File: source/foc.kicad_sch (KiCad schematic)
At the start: 22 parts

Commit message: Add files via upload
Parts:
- gave numbers to parts that had none: 22
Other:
- sheet mcu ports: added none; removed ADC_15, ADC_TEMP2, ADC_TEMP3, MISO_ADC_EXT2, PC10_UART_TX, PC11_UART_RX, PC12, PC9, RX_SDA_NSS, SCK_ADC_EXT, TX_SCL_MOSI

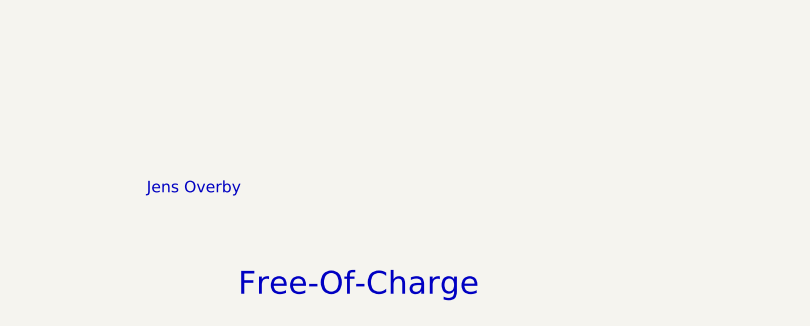
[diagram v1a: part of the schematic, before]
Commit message: Changes suggested by mxlemming, Elwin and hackey on Discord
New power supplies and using other op-amps for current sense
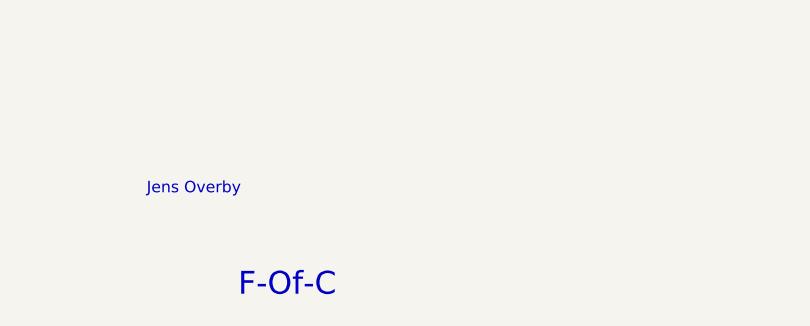
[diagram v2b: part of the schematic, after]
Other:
- note added: "F-Of-C"
- note removed: "Free-Of-Charge"

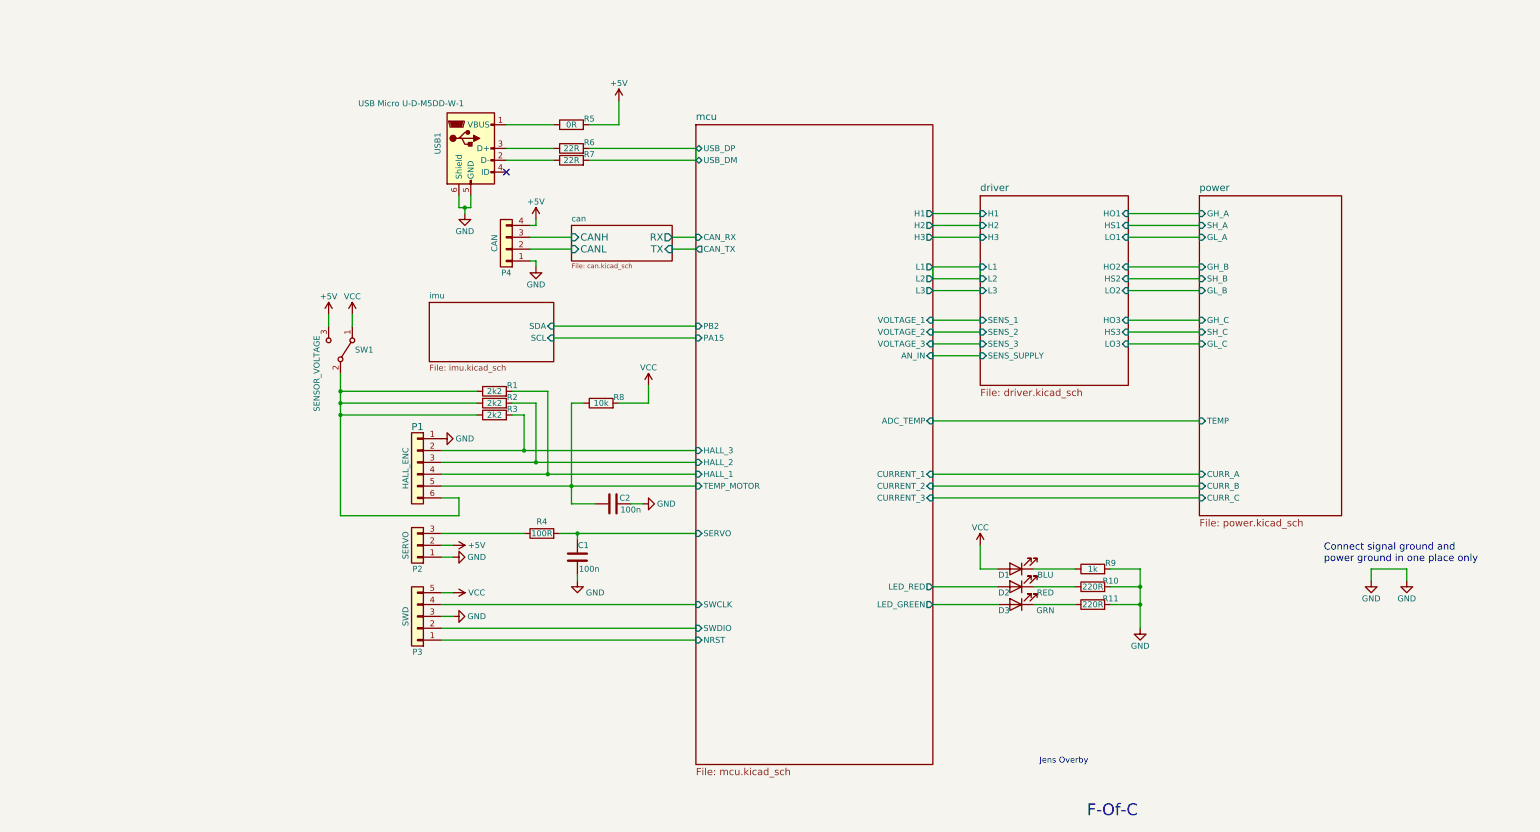
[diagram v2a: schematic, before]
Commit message: First attempt of layout
It's a rats nest. Will have to remove some connections temporarily for the first prototype.
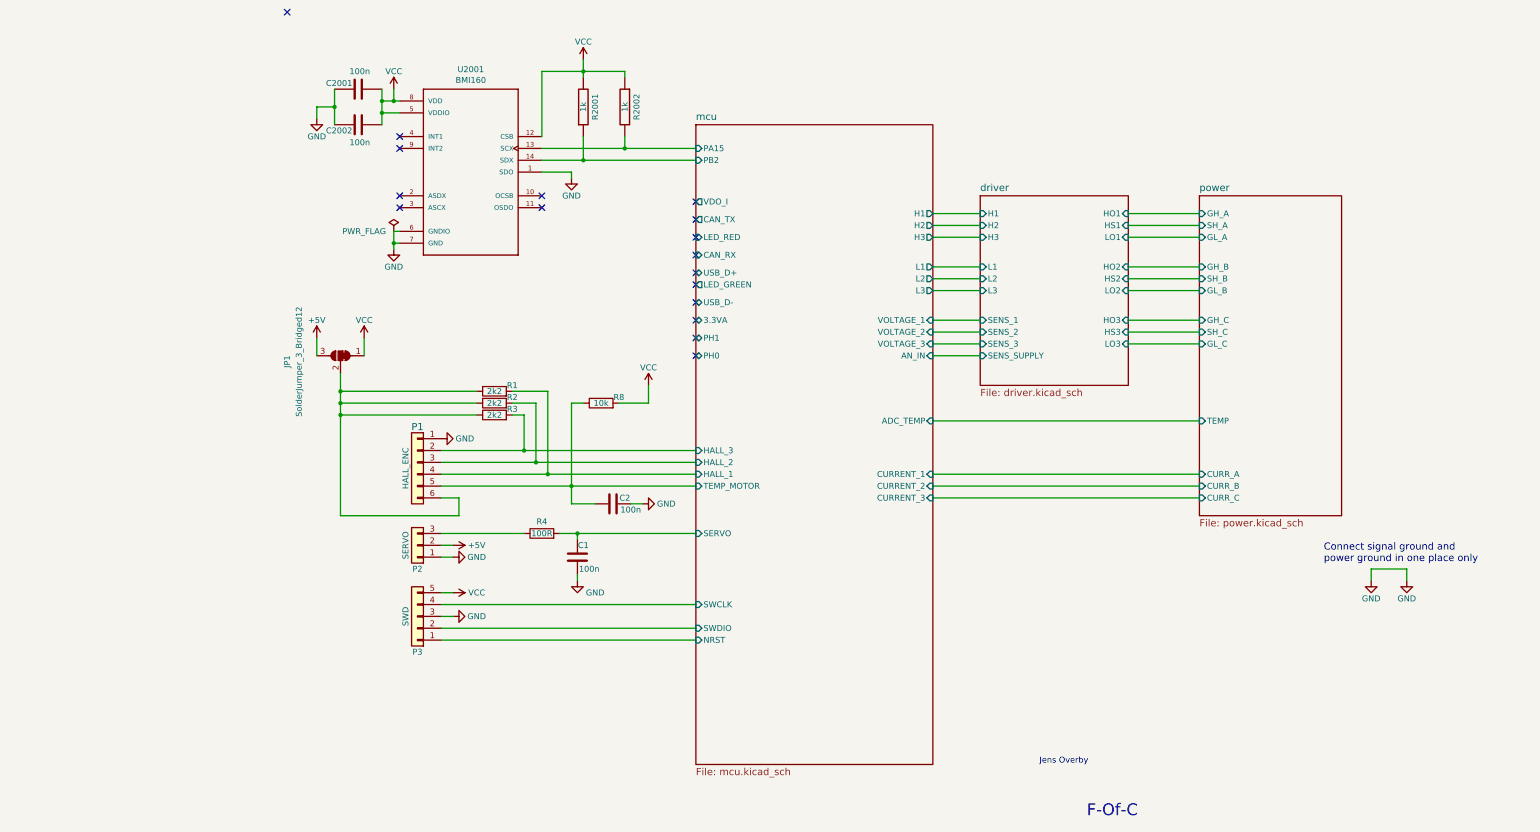
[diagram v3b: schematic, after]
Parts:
- removed D1: BLU, LED_SMD:LED_0603_1608Metric, symbol Device:LED
- removed D2: RED, LED_SMD:LED_0603_1608Metric, symbol Device:LED
- removed D3: GRN, LED_SMD:LED_0603_1608Metric, symbol Device:LED
- removed P4: CAN, symbol Connector_Generic:Conn_01x04
- removed R10, R11: 220R, symbol Device:R
- removed R5: 0R, symbol Device:R
- removed R6, R7: 22R, symbol Device:R
- removed R9: 1k, symbol Device:R
- removed SW1: SENSOR_VOLTAGE, Button_Switch_THT:SW_E-Switch_EG1224_SPDT_Angled, symbol Switch:SW_SPDT
- removed USB1: USB Micro U-D-M5DD-W-1, Connector_USB:USB_Micro-B_Wuerth_614105150721_Vertical, symbol Connector:USB_B_Micro
- added C2001, C2002: 100n, Capacitor_SMD:C_0603_1608Metric, symbol BLDC_4-rescue:C-RESCUE-BLDC_4
- added JP1: SolderJumper_3_Bridged12, Jumper:SolderJumper-3_P1.3mm_Bridged12_RoundedPad1.0x1.5mm_NumberLabels, symbol Jumper:SolderJumper_3_Bridged12
- added R2001, R2002: 1k, Resistor_SMD:R_0402_1005Metric, symbol BLDC_4-rescue:R-RESCUE-BLDC_4
- added U2001: BMI160, Package_LGA:Bosch_LGA-14_3x2.5mm_P0.5mm, symbol Cheap-FOCer-2-60mm-rescue:BMI160-IMU
- C1, C2: footprint (none) -> Capacitor_SMD:C_0603_1608Metric
- P1: footprint Connector_JST:JST_PH_B6B-PH-K_1x06_P2.00mm_Vertical -> Connector_PinHeader_2.54mm:PinHeader_1x06_P2.54mm_Vertical
- P2: footprint (none) -> Connector_PinHeader_2.54mm:PinHeader_1x03_P2.54mm_Vertical
- P3: footprint (none) -> Connector_PinHeader_2.54mm:PinHeader_1x05_P2.54mm_Vertical
- R1, R2, R3, R4, R8: footprint (none) -> Resistor_SMD:R_0402_1005Metric
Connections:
- net +5V: now also JP1.3 (B)
- net GND: now also C2001.1, C2002.1, U2001.1 (SDO), U2001.6 (GNDIO), U2001.7 (GND)
- net VCC: now also C2001.2, C2002.2, JP1.1 (A), R2001.2, R2002.1, U2001.12 (CSB), U2001.5 (VDDIO), U2001.8 (VDD)
- net at P1.6 (Pin_6), R1.1, R2.1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: now also JP1.2 (C)
- new net mcu/PA15: R2002.2, U2001.13 (SCX)
- new net mcu/PB2: R2001.1, U2001.14 (SDX)
- no-connect marks 1 -> 17
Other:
- removed sheet can
- removed sheet imu
- sheet mcu ports: added 3.3VA, PH0, PH1, USB_D+, USB_D-, VDO_I; removed USB_DM, USB_DP

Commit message: Most components now jlcpcb basic
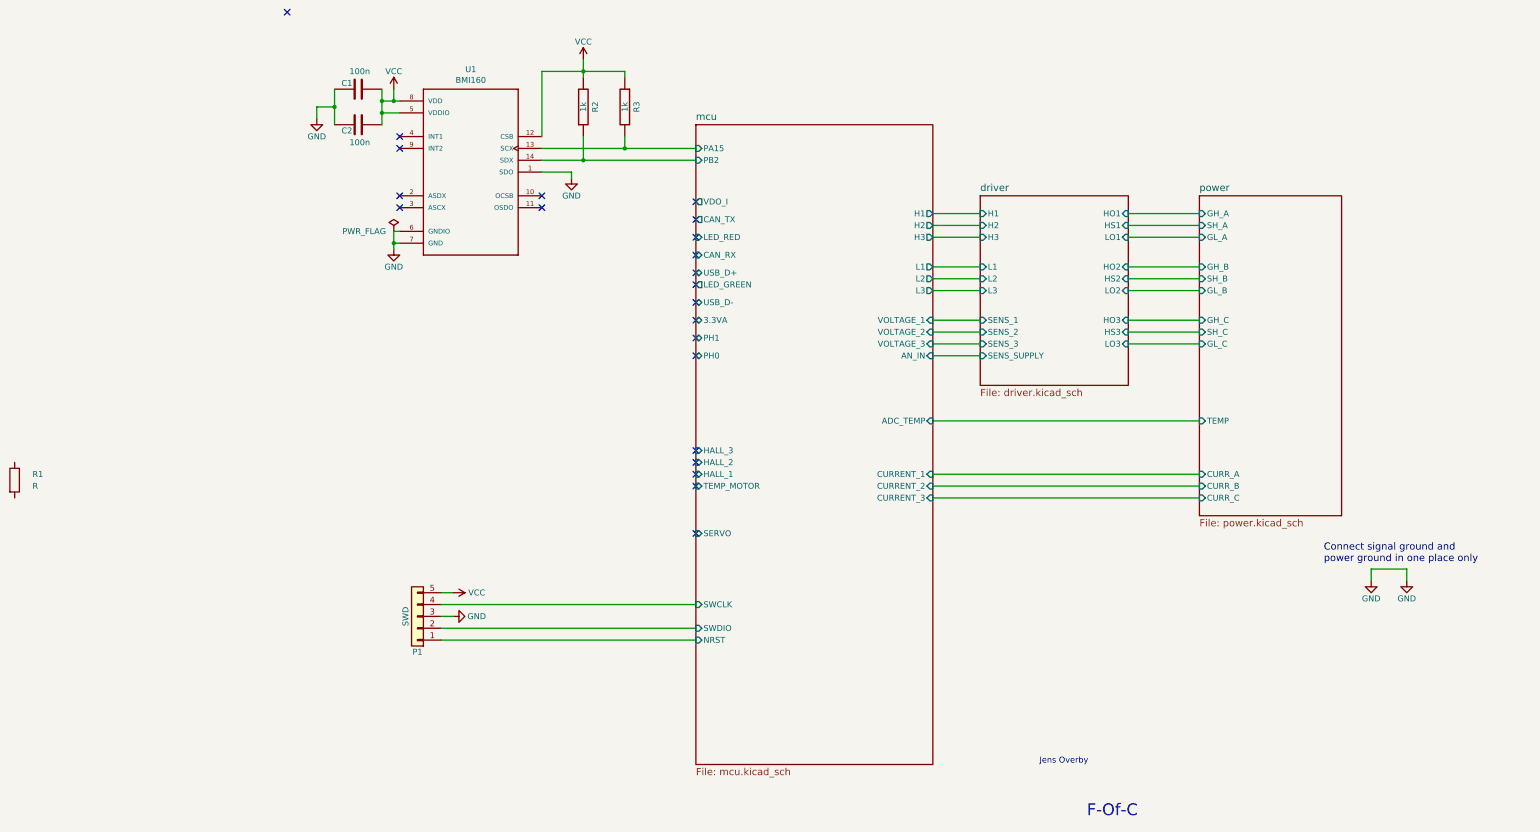
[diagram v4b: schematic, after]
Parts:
- removed C1, C2: 100n, Capacitor_SMD:C_0603_1608Metric, symbol Device:C
- removed JP1: SolderJumper_3_Bridged12, Jumper:SolderJumper-3_P1.3mm_Bridged12_RoundedPad1.0x1.5mm_NumberLabels, symbol Jumper:SolderJumper_3_Bridged12
- removed P1: HALL_ENC, Connector_PinHeader_2.54mm:PinHeader_1x06_P2.54mm_Vertical, symbol Connector_Generic:Conn_01x06
- removed P2: SERVO, Connector_PinHeader_2.54mm:PinHeader_1x03_P2.54mm_Vertical, symbol Connector_Generic:Conn_01x03
- removed R2, R3: 2k2, Resistor_SMD:R_0402_1005Metric, symbol Device:R
- removed R4: 100R, Resistor_SMD:R_0402_1005Metric, symbol Device:R
- removed R8: 10k, Resistor_SMD:R_0402_1005Metric, symbol Device:R
- C1: renamed from C2001; footprint Capacitor_SMD:C_0603_1608Metric -> Capacitor_SMD:C_0402_1005Metric; LCSC (none) -> C1525
- C2: renamed from C2002; footprint Capacitor_SMD:C_0603_1608Metric -> Capacitor_SMD:C_0402_1005Metric; LCSC (none) -> C1525
- R1: value 2k2 -> R; footprint Resistor_SMD:R_0402_1005Metric -> Custom:field
- R2: renamed from R2001; LCSC (none) -> C11702
- R3: renamed from R2002; LCSC (none) -> C11702
- U1: renamed from U2001; LCSC (none) -> C94021
- renumbered P3 to P1
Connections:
- net mcu/HALL_1: no longer R1.2
- no-connect marks 17 -> 22

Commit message: Add files via upload
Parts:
- renumbered R1 to FieldFeets
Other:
- moved on the sheet: FieldFeets
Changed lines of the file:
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@@
     (pin "9")
   )
-  (symbol (lib_id "Device:R") (at -41.91 119.38 0) (unit 1)
+  (symbol (lib_id "Device:R") (at 53.34 109.22 0) (unit 1)
     (in_bom yes) (on_board yes) (fields_autoplaced)
-    (property "Reference" "R1" (id 0) (at -38.1 118.1099 0)
-      (effects (font (size 1.27 1.27)) (justify left))
-    )
-    (property "Value" "R" (id 1) (at -38.1 120.6499 0)
-      (effects (font (size 1.27 1.27)) (justify left))
-    )
-    (property "Footprint" "Custom:field" (id 2) (at -43.688 119.38 90)
-      (effects (font (size 1.27 1.27)) hide)
-    )
-    (property "Datasheet" "~" (id 3) (at -41.91 119.38 0)
+    (property "Reference" "FieldFeets" (id 0) (at 55.88 107.9499 0)
+      (effects (font (size 1.27 1.27)) (justify left))
+    )
+    (property "Value" "R" (id 1) (at 55.88 110.4899 0)
+      (effects (font (size 1.27 1.27)) (justify left))
+    )
+    (property "Footprint" "Custom:field" (id 2) (at 51.562 109.22 90)
+      (effects (font (size 1.27 1.27)) hide)
+    )
+    (property "Datasheet" "~" (id 3) (at 53.34 109.22 0)
       (effects (font (size 1.27 1.27)) hide)
     )
@@
       (reference "D18") (unit 1) (value "BLU") (footprint "LED_SMD:LED_0603_1608Metric")
     )
+    (path "/62ef4635-b49c-438c-85be-c661ac8e24f3"
+      (reference "FieldFeets") (unit 1) (value "R") (footprint "Custom:field")
+    )
     (path "/64b117fb-212c-4b17-8f2f-7c4db3eb0d00/f60dae52-c28c-46c1-b027-f3d548cb9533"
       (reference "J1") (unit 1) (value "Conn_01x04_Male") (footprint "Connector_PinHeader_2.54mm:PinHeader_1x04_P2.54mm_Vertical")
@@
       (reference "Q18") (unit 1) (value "CSD19536KCS") (footprint "Package_TO_SOT_THT:TO-220-3_Vertical")
     )
-    (path "/62ef4635-b49c-438c-85be-c661ac8e24f3"
-      (reference "R1") (unit 1) (value "R") (footprint "Custom:field")
-    )
     (path "/61335856-a61f-49fc-8440-5f9d8f38f7e0"

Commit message: Add files via upload
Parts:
- C1, C2: footprint Capacitor_SMD:C_0402_1005Metric -> Capacitor_SMD:C_0603_1608Metric; LCSC C1525 -> C14663
- R1: renamed from R2; footprint Resistor_SMD:R_0402_1005Metric -> Resistor_SMD:R_0603_1608Metric; LCSC C11702 -> C21190
- R2: renamed from R3; footprint Resistor_SMD:R_0402_1005Metric -> Resistor_SMD:R_0603_1608Metric; LCSC C11702 -> C21190
- renumbered FieldFeets to FieldFeets1
